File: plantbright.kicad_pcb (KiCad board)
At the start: 2 copper layers, 4 parts, among them Q1 CHANNEL 1, Q2 CHANNEL 2, Q3 CHANNEL 3, U1 XIAO-ESP32-C6

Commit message: Start board layout
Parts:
- added J3: USB_C_Receptacle_USB2.0_14P, Connector_USB:USB_C_Receptacle_HRO_TYPE-C-31-M-12, F.Cu at (134.1, 108.1)
- added Q4: AO3400A, Package_TO_SOT_SMD:SOT-23-3, F.Cu at (151.2, 94.2)
- added Q5: AO3400A, Package_TO_SOT_SMD:SOT-23-3, F.Cu at (151.2, 98.7)
- added R1: 100R, Resistor_SMD:R_0805_2012Metric_Pad1.20x1.40mm_HandSolder, F.Cu at (151.0, 102.4)
- added R10: 10K, Resistor_SMD:R_0805_2012Metric_Pad1.20x1.40mm_HandSolder, F.Cu at (155.8, 114.2)
- added R11: 10K, Resistor_SMD:R_0805_2012Metric_Pad1.20x1.40mm_HandSolder, F.Cu at (160.5, 102.4)
- added R12: 10K, Resistor_SMD:R_0805_2012Metric_Pad1.20x1.40mm_HandSolder, F.Cu at (160.5, 105.3)
- added R13: 5.1K, Resistor_SMD:R_0805_2012Metric_Pad1.20x1.40mm_HandSolder, F.Cu at (160.5, 108.3)
- added R14: 5.1K, Resistor_SMD:R_0805_2012Metric_Pad1.20x1.40mm_HandSolder, F.Cu at (160.5, 111.2)
- added R2: 10K, Resistor_SMD:R_0805_2012Metric_Pad1.20x1.40mm_HandSolder, F.Cu at (151.0, 105.3)
- added R3: 100R, Resistor_SMD:R_0805_2012Metric_Pad1.20x1.40mm_HandSolder, F.Cu at (151.0, 108.3)
- added R4: 10K, Resistor_SMD:R_0805_2012Metric_Pad1.20x1.40mm_HandSolder, F.Cu at (151.0, 111.2)
- added R5: 100R, Resistor_SMD:R_0805_2012Metric_Pad1.20x1.40mm_HandSolder, F.Cu at (151.0, 114.2)
- added R6: 10K, Resistor_SMD:R_0805_2012Metric_Pad1.20x1.40mm_HandSolder, F.Cu at (155.8, 102.4)
- added R7: 100R, Resistor_SMD:R_0805_2012Metric_Pad1.20x1.40mm_HandSolder, F.Cu at (155.8, 105.3)
- added R8: 10K, Resistor_SMD:R_0805_2012Metric_Pad1.20x1.40mm_HandSolder, F.Cu at (155.8, 108.3)
- added R9: 100R, Resistor_SMD:R_0805_2012Metric_Pad1.20x1.40mm_HandSolder, F.Cu at (155.8, 111.2)
- added SW1: SW_Push, Button_Switch_THT:SW_PUSH_6mm, F.Cu at (168.0, 81.8)
- added SW2: SW_Push, Button_Switch_THT:SW_PUSH_6mm, F.Cu at (168.0, 93.0)
- Q1: value CHANNEL 1 -> AO3400A; footprint Package_TO_SOT_SMD:SOT-23 -> Package_TO_SOT_SMD:SOT-23-3
- Q2: value CHANNEL 2 -> AO3400A; footprint Package_TO_SOT_SMD:SOT-23 -> Package_TO_SOT_SMD:SOT-23-3
- Q3: value CHANNEL 3 -> AO3400A; footprint Package_TO_SOT_SMD:SOT-23 -> Package_TO_SOT_SMD:SOT-23-3
- moved U1 28.8 mm to (123.3, 89.8)
- moved Q3 24.5 mm to (151.2, 89.8)
- moved Q2 23.0 mm to (151.2, 85.3)
- moved Q1 22.1 mm to (151.2, 80.9)
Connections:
- Q1 pad 1: unconnected-(Q1-G-Pad1) -> Net-(Q1-G)
- Q1 pad 2: unconnected-(Q1-S-Pad2) -> GND
- Q1 pad 3: unconnected-(Q1-D-Pad3) -> SW_1
- Q2 pad 1: unconnected-(Q2-G-Pad1) -> Net-(Q2-G)
- Q2 pad 2: unconnected-(Q2-S-Pad2) -> GND
- Q2 pad 3: unconnected-(Q2-D-Pad3) -> SW_2
- Q3 pad 1: unconnected-(Q3-G-Pad1) -> Net-(Q3-G)
- Q3 pad 2: unconnected-(Q3-S-Pad2) -> GND
- Q3 pad 3: unconnected-(Q3-D-Pad3) -> SW_3
- U1 pad 1: unconnected-(U1-GPIO0/A0/D0-Pad1) -> CH_1
- U1 pad 10: unconnected-(U1-GPIO20/D9/MISO-Pad10) -> CH_5
- U1 pad 11: unconnected-(U1-GPIO18/D10/MOSI-Pad11) -> CH_4
- U1 pad 12: unconnected-(U1-3V3-Pad12) -> +3.3V
- U1 pad 2: unconnected-(U1-GPIO1/A1/D1-Pad2) -> CH_2
- U1 pad 3: unconnected-(U1-GPIO2/A2/D2-Pad3) -> CH_3
- U1 pad 4: unconnected-(U1-GPIO21/D3-Pad4) -> CH_3
- U1 pad 5: unconnected-(U1-GPIO22/D4/SDA-Pad5) -> BTN_1
- U1 pad 6: unconnected-(U1-GPIO23/D5/SCL-Pad6) -> BTN_2
- U1 pad 7: unconnected-(U1-GPIO16/D6/TX-Pad7) -> DF_RX
- U1 pad 8: unconnected-(U1-GPIO17/D7/RX-Pad8) -> DF_TX
- U1 pad 9: unconnected-(U1-GPIO19/D8/SCK-Pad9) -> BUSY

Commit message: Enough for now. Arranging bits.
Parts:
- added J1: POWER OUT, Connector_JST:JST_XH_B6B-XH-A_1x06_P2.50mm_Vertical, F.Cu at (97.0, 68.9)
- added J2: SPEAKER, Connector_JST:JST_XH_B2B-XH-A_1x02_P2.50mm_Vertical, F.Cu at (125.8, 69.0)
- SW1: value SW_Push -> USER 0
- SW2: value SW_Push -> USER 1
- moved SW1 87.5 mm to (82.8, 101.5)
- moved SW2 70.5 mm to (98.0, 101.5)
- moved R11 67.0 mm to (93.5, 104.2), turned to -90 degrees
- moved R12 51.8 mm to (108.8, 104.2), turned to -90 degrees
- moved R13 46.2 mm to (114.8, 101.6), turned to -90 degrees
- moved R14 46.0 mm to (114.8, 105.8), turned to -90 degrees
- moved U1 31.7 mm to (91.6, 88.9), turned to -90 degrees
- moved Q1 18.2 mm to (136.9, 69.7)
- moved Q2 18.2 mm to (136.9, 74.1)
- moved Q3 18.2 mm to (136.9, 78.5)
- moved Q4 18.2 mm to (136.9, 83.0)
- moved Q5 18.2 mm to (136.9, 87.5)
- moved R1 18.2 mm to (136.8, 91.2)
- moved R10 18.2 mm to (141.5, 103.0)
- moved R2 18.2 mm to (136.8, 94.1)
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
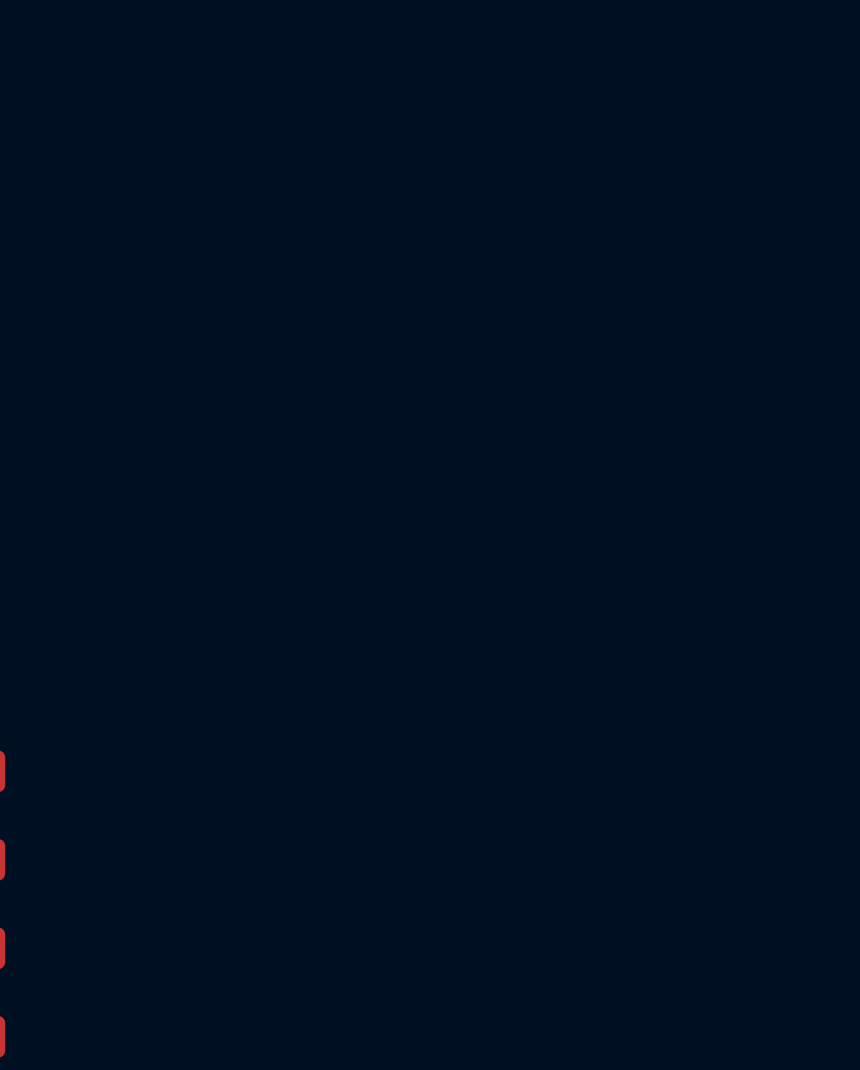
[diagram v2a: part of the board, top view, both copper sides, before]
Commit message: Add in dfplayermini board.
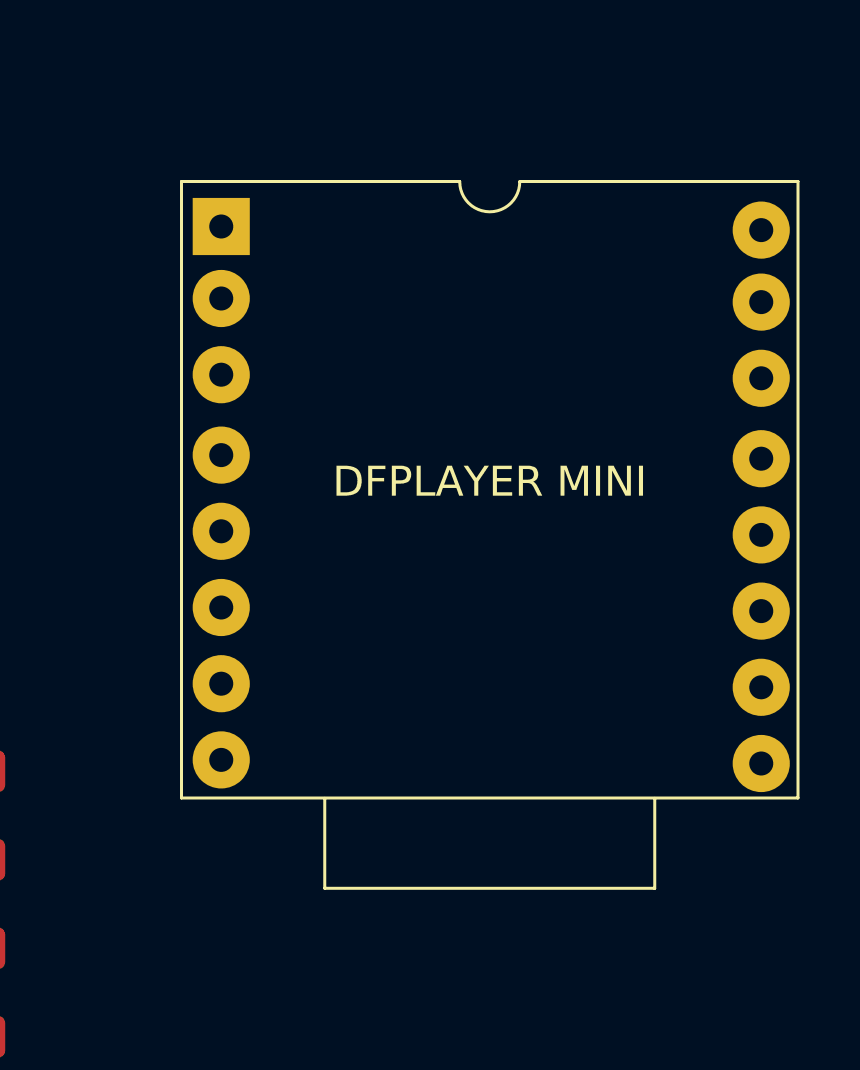
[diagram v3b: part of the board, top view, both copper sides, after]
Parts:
- added U2: DFPLAYER MINI, kicad-dfplayermini:dfplayer, F.Cu at (159.2, 63.5)
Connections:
- J2 pad 1: DF_L -> DF+
- J2 pad 2: DF_R -> DF-

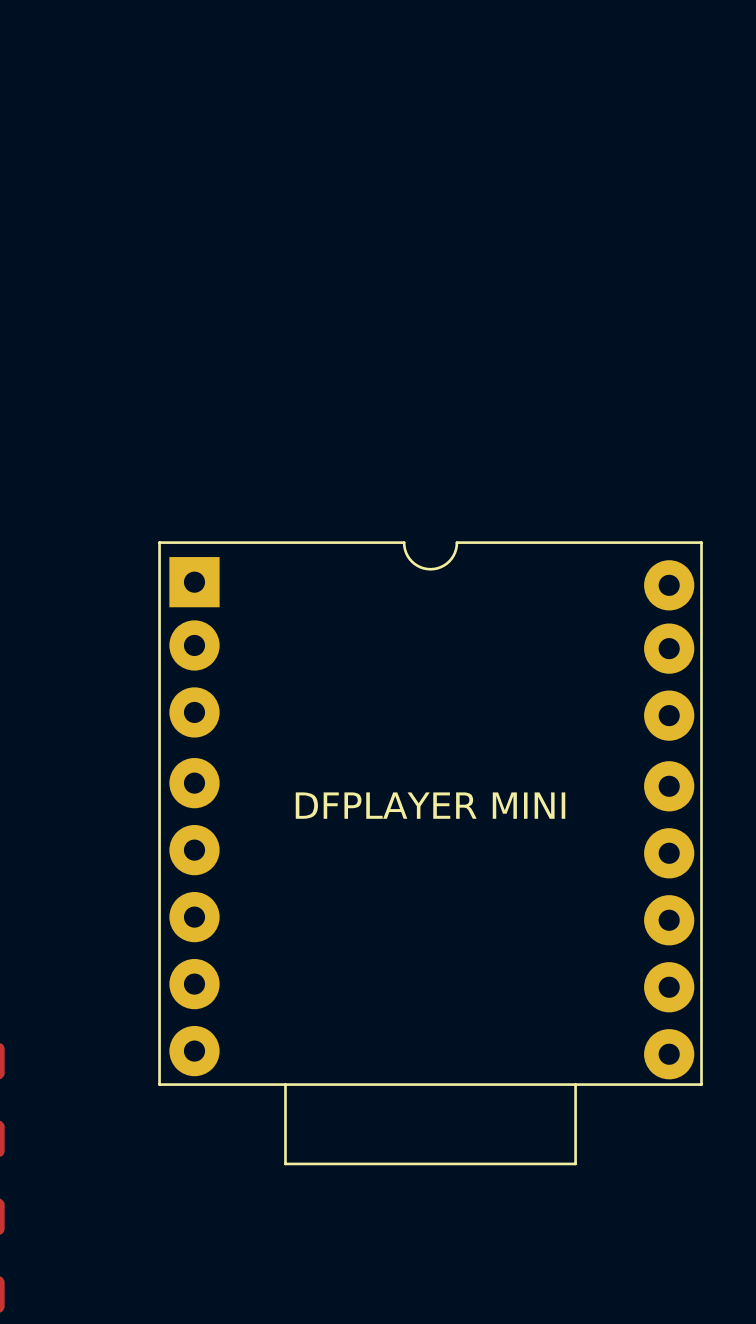
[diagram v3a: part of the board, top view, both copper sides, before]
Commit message: Update `dfmini` library
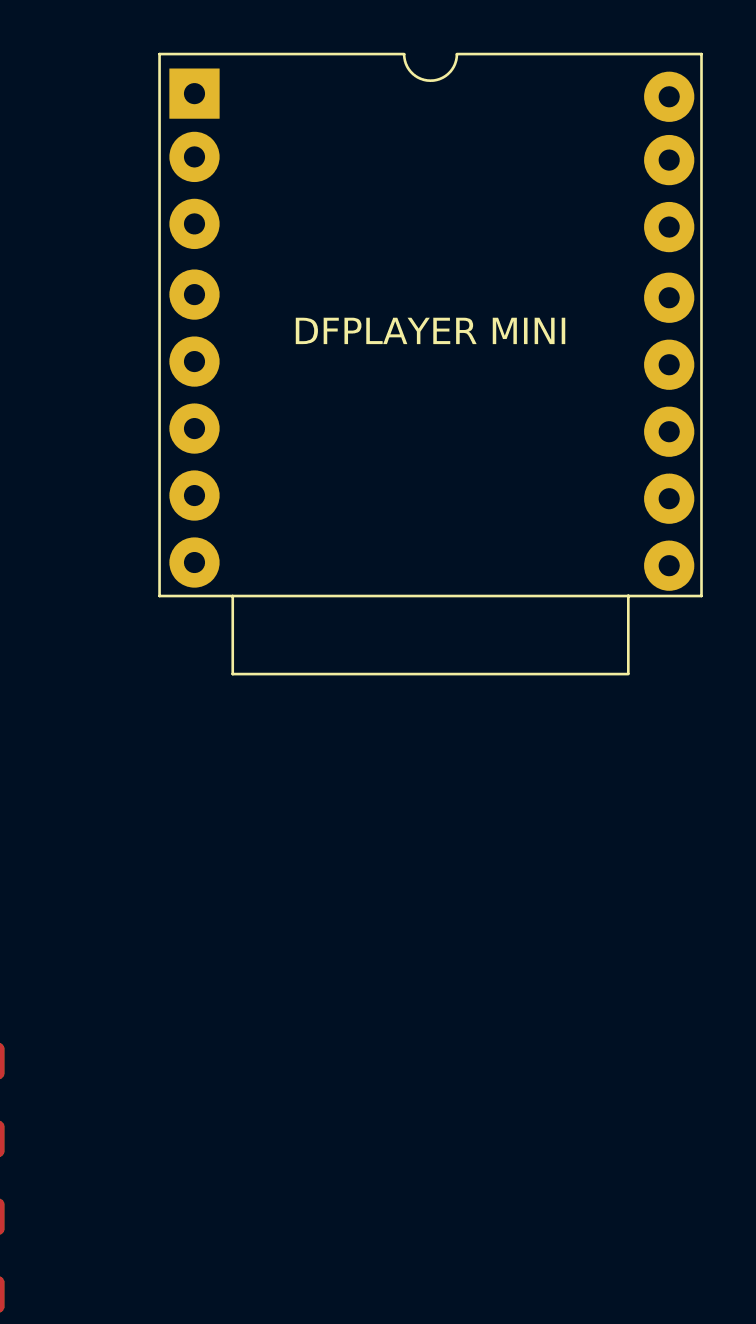
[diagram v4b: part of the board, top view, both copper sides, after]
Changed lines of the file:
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@@
 		)
 		(property "Value" "DFPLAYER MINI"
-			(at 0 18 0)
+			(at 0 0 0)
 			(unlocked yes)
 			(layer "F.SilkS")
@@
 		(attr smd)
 		(fp_line
-			(start -10.275 7.99)
-			(end -10.275 28.54)
-			(stroke
-				(width 0.1)
-				(type default)
-			)
-			(layer "F.SilkS")
-		)
-		(fp_line
-			(start -10.275 28.54)
-			(end 10.275 28.54)
-			(stroke
-				(width 0.1)
-				(type default)
-			)
-			(layer "F.SilkS")
-		)
-		(fp_line
-			(start -5.5 28.55)
-			(end -5.5 31.55)
-			(stroke
-				(width 0.1)
-				(type default)
-			)
-			(layer "F.SilkS")
-		)
-		(fp_line
-			(start -5.5 31.55)
-			(end 5.5 31.55)
-			(stroke
-				(width 0.1)
-				(type default)
-			)
-			(layer "F.SilkS")
-		)
-		(fp_line
-			(start -0.999949 7.989901)
-			(end -10.275 7.99)
-			(stroke
-				(width 0.1)
-				(type default)
-			)
-			(layer "F.SilkS")
-		)
-		(fp_line
-			(start 0.999949 7.99)
-			(end 10.275 7.99)
-			(stroke
-				(width 0.1)
-				(type default)
-			)
-			(layer "F.SilkS")
-		)
-		(fp_line
-			(start 5.5 31.55)
-			(end 5.5 28.55)
-			(stroke
-				(width 0.1)
-				(type default)
-			)
-			(layer "F.SilkS")
-		)
-		(fp_line
-			(start 10.275 7.99)
-			(end 10.275 28.54)
+			(start -10.275 -10.535)
+			(end -10.275 10.015)
+			(stroke
+				(width 0.1)
+				(type default)
+			)
+			(layer "F.SilkS")
+		)
+		(fp_line
+			(start -10.275 10.015)
+			(end 10.275 10.015)
+			(stroke
+				(width 0.1)
+				(type default)
+			)
+			(layer "F.SilkS")
+		)
+		(fp_line
+			(start -7.5 10.015)
+			(end -7.5 12.975)
+			(stroke
+				(width 0.1)
+				(type default)
+			)
+			(layer "F.SilkS")
+		)
+		(fp_line
+			(start -7.5 12.975)
+			(end 7.5 12.975)
+			(stroke
+				(width 0.1)
+				(type default)
+			)
+			(layer "F.SilkS")
+		)
+		(fp_line
+			(start -0.999949 -10.535099)
+			(end -10.275 -10.535)
+			(stroke
+				(width 0.1)
+				(type default)
+			)
+			(layer "F.SilkS")
+		)
+		(fp_line
+			(start 0.999949 -10.535)
+			(end 10.275 -10.535)
+			(stroke
+				(width 0.1)
+				(type default)
+			)
+			(layer "F.SilkS")
+		)
+		(fp_line
+			(start 7.5 12.95)
+			(end 7.5 10)
+			(stroke
+				(width 0.1)
+				(type default)
+			)
+			(layer "F.SilkS")
+		)
+		(fp_line
+			(start 10.275 -10.535)
+			(end 10.275 10.015)
 			(stroke
 				(width 0.1)
@@
 		)
 		(fp_arc
-			(start 1 8)
-			(mid 0 9)
-			(end -1 8)
+			(start 1 -10.525)
+			(mid 0 -9.525)
+			(end -1 -10.525)
 			(stroke
 				(width 0.1)
@@
 		)
 		(pad "1" thru_hole rect
-			(at -8.95 9.49 90)
+			(at -8.95 -9.035 90)
 			(size 1.905 1.905)
 			(drill 0.8)
@@
 		)
 		(pad "2" thru_hole circle
-			(at -8.95 11.89 90)
+			(at -8.95 -6.635 90)
 			(size 1.905 1.905)
 			(drill 0.8)
@@
 		)
 		(pad "3" thru_hole circle
-			(at -8.95 14.43 90)
+			(at -8.95 -4.095 90)
 			(size 1.905 1.905)
 			(drill 0.8)
@@
 		)
 		(pad "4" thru_hole circle
-			(at -8.95 17.11 90)
+			(at -8.95 -1.415 90)
 			(size 1.905 1.905)
 			(drill 0.8)
@@
 		)
 		(pad "5" thru_hole circle
-			(at -8.95 19.65 90)
+			(at -8.95 1.125 90)
 			(size 1.905 1.905)
 			(drill 0.8)
@@
 		)
 		(pad "6" thru_hole circle
-			(at -8.95 22.19 90)
+			(at -8.95 3.665 90)
 			(size 1.905 1.905)
 			(drill 0.8)
@@
 		)
 		(pad "7" thru_hole circle
-			(at -8.95 24.73 90)
+			(at -8.95 6.205 90)
 			(size 1.905 1.905)
 			(drill 0.8)
@@
 		)
 		(pad "8" thru_hole circle
-			(at -8.95 27.27 90)
+			(at -8.95 8.745 90)
 			(size 1.905 1.905)
 			(drill 0.8)
@@
 		)
 		(pad "9" thru_hole circle
-			(at 9.05 9.61 90)
+			(at 9.05 -8.915 90)
 			(size 1.905 1.905)
 			(drill 0.8)
@@
 		)
 		(pad "10" thru_hole circle
-			(at 9.05 12.01 90)
+			(at 9.05 -6.515 90)
 			(size 1.905 1.905)
 			(drill 0.8)
@@
 		)
 		(pad "11" thru_hole circle
-			(at 9.05 14.55 90)
+			(at 9.05 -3.975 90)
 			(size 1.905 1.905)
 			(drill 0.8)
@@
 		)
 		(pad "12" thru_hole circle
-			(at 9.05 17.23 90)
+			(at 9.05 -1.295 90)
 			(size 1.905 1.905)
 			(drill 0.8)
@@
 		)
 		(pad "13" thru_hole circle
-			(at 9.05 19.77 90)
+			(at 9.05 1.245 90)
 			(size 1.905 1.905)
 			(drill 0.8)
@@
 		)
 		(pad "14" thru_hole circle
-			(at 9.05 22.31 90)
+			(at 9.05 3.785 90)
 			(size 1.905 1.905)
 			(drill 0.8)
@@
 		)
 		(pad "15" thru_hole circle
-			(at 9.05 24.85 90)
+			(at 9.05 6.325 90)
 			(size 1.905 1.905)
 			(drill 0.8)
@@
 		)
 		(pad "16" thru_hole circle
-			(at 9.05 27.39 90)
-			(size 1.905 1.905)
-			(drill 0.8)
+			(at 9.05 8.865 90)
+			(size 1.905 1.905)
+			(drill 0.8)

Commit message: Start layout again
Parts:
- removed J3: USB_C_Receptacle_USB2.0_14P, Connector_USB:USB_C_Receptacle_HRO_TYPE-C-31-M-12
- removed R13, R14: 5.1K, Resistor_SMD:R_0805_2012Metric_Pad1.20x1.40mm_HandSolder
- added J4: 5V IN, Connector_JST:JST_XH_B2B-XH-A_1x02_P2.50mm_Vertical, F.Cu at (136.2, 69.2)
- Q1, Q2, Q3, Q4, Q5: footprint Package_TO_SOT_SMD:SOT-23-3 -> Package_TO_SOT_SMD:SOT-23
- moved Q2 95.5 mm to (42.0, 84.7), turned to -90 degrees
- moved Q1 91.9 mm to (46.2, 84.7), turned to -90 degrees
- moved Q3 86.7 mm to (50.5, 84.8), turned to -90 degrees
- moved Q4 82.2 mm to (54.8, 84.8), turned to -90 degrees
- moved Q5 78.0 mm to (59.0, 84.8), turned to -90 degrees
- moved R1 68.7 mm to (68.2, 96.9)
- moved R10 68.7 mm to (73.0, 108.7)
- moved R2 68.7 mm to (68.2, 99.8)
- moved R3 68.7 mm to (68.2, 102.8)
- moved R4 68.7 mm to (68.2, 105.8)
- moved R5 68.7 mm to (68.2, 108.7)
- moved R6 68.7 mm to (73.0, 96.9)
- moved R7 68.7 mm to (73.0, 99.8)
- moved R8 68.7 mm to (73.0, 102.8)
- moved R9 68.7 mm to (73.0, 105.8)
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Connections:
- U2 pad 14: GND -> unconnected-(U2-IO_2-Pad14)
- U2 pad 15: unconnected-(U2-IO_1-Pad15) -> GND
- U2 pad 16: (no net) -> unconnected-(U2-IO_1-Pad16)
- U2 pad 5: DF+ -> unconnected-(U2-DAC_L-Pad5)
- U2 pad 6: GND -> DF+
- U2 pad 7: DF- -> GND
- U2 pad 8: BUSY -> DF-
- U2 pad 9: unconnected-(U2-D--Pad9) -> BUSY
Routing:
- net BTN_2: track 0.00 -> 11.5 mm
- net BTN_1: track 0.00 -> 11.5 mm

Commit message: Layout
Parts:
- moved R12 171.1 mm to (12.4, 3.92), turned to 0 degrees
- moved R11 166.7 mm to (12.4, 0.97), turned to 0 degrees
- moved SW2 166.3 mm to (1.52, 10.1)
- moved SW1 165.1 mm to (1.52, 1.52)
- moved U1 147.3 mm to (193.8, 95.2), turned to 90 degrees
- moved Q2 103.0 mm to (144.8, 77.1), turned to 90 degrees
- moved Q5 99.5 mm to (158.2, 77.1), turned to 90 degrees
- moved Q4 99.3 mm to (153.8, 77.1), turned to 90 degrees
- moved Q3 99.1 mm to (149.3, 77.1), turned to 90 degrees
- moved Q1 94.3 mm to (140.2, 77.1), turned to 90 degrees
- moved R10 66.8 mm to (136.0, 86.5)
- moved R9 64.0 mm to (135.0, 90.0), turned to 90 degrees
- moved R5 59.9 mm to (123.7, 86.1)
- moved R7 57.9 mm to (129.2, 86.1)
- moved R8 57.6 mm to (129.2, 90.1)
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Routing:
- net BTN_2: track 11.5 -> 0.00 mm
- net BTN_1: track 11.5 -> 0.00 mm
